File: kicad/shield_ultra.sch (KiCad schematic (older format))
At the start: 12 parts, among them J1 Ultrason, J2 IR, J3 Accel, J4 IR, J5 Ultrason, J6 IR, J7 Ultrason, J8 Ultrason, J9 Ultrason, U1 Conn_shield

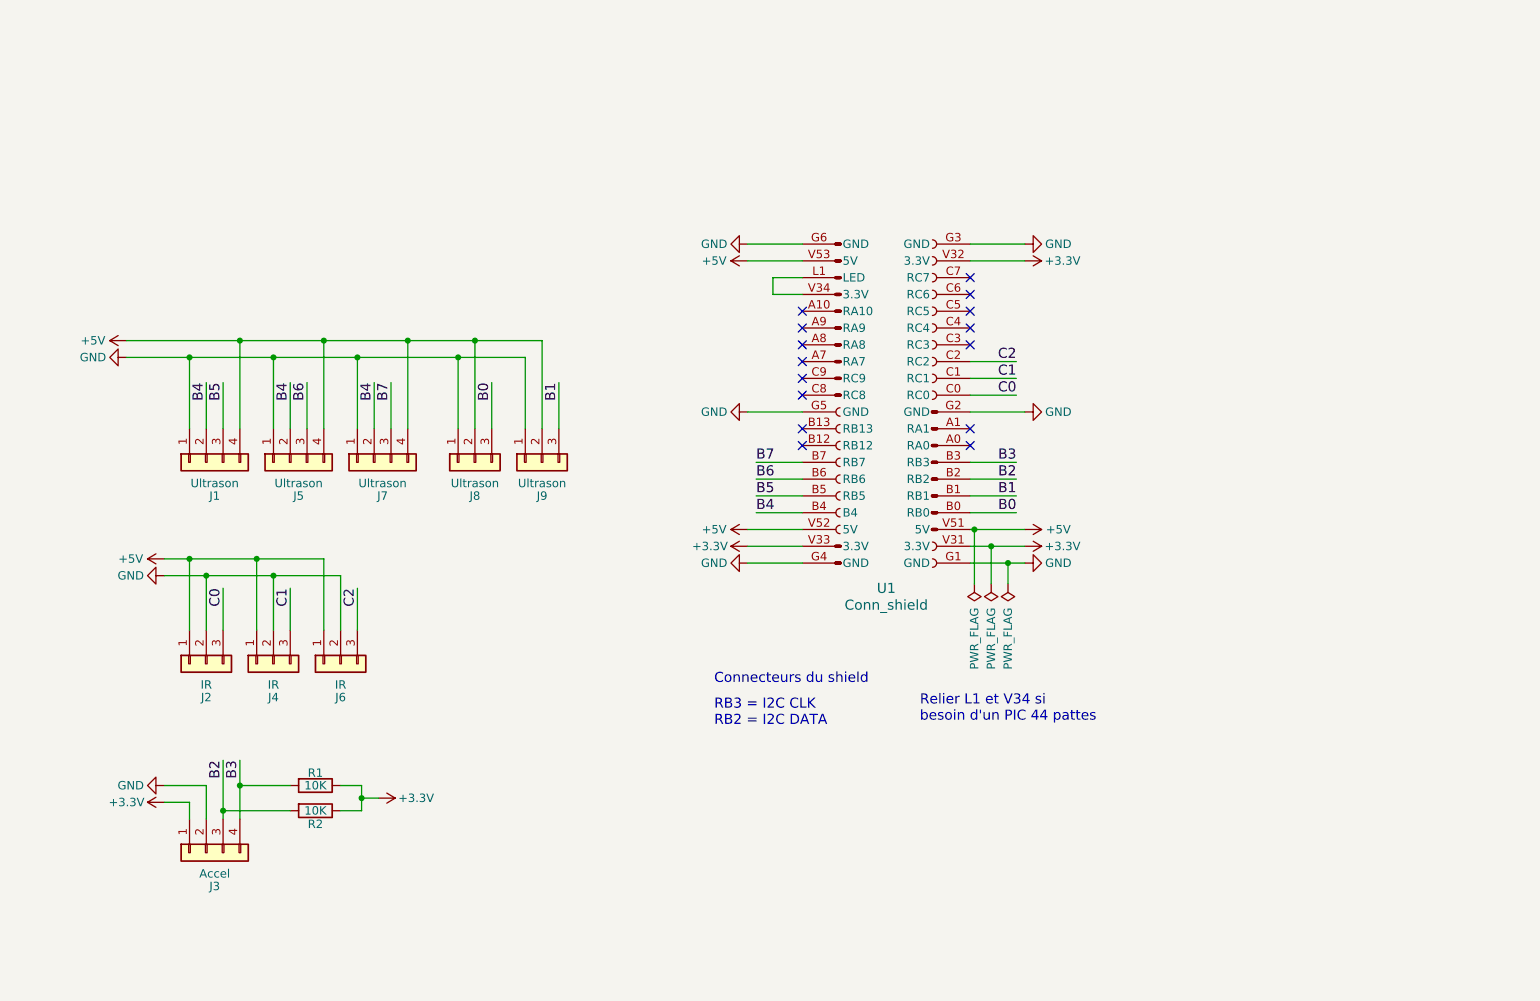
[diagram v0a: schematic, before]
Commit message: Modification connexions capteurs
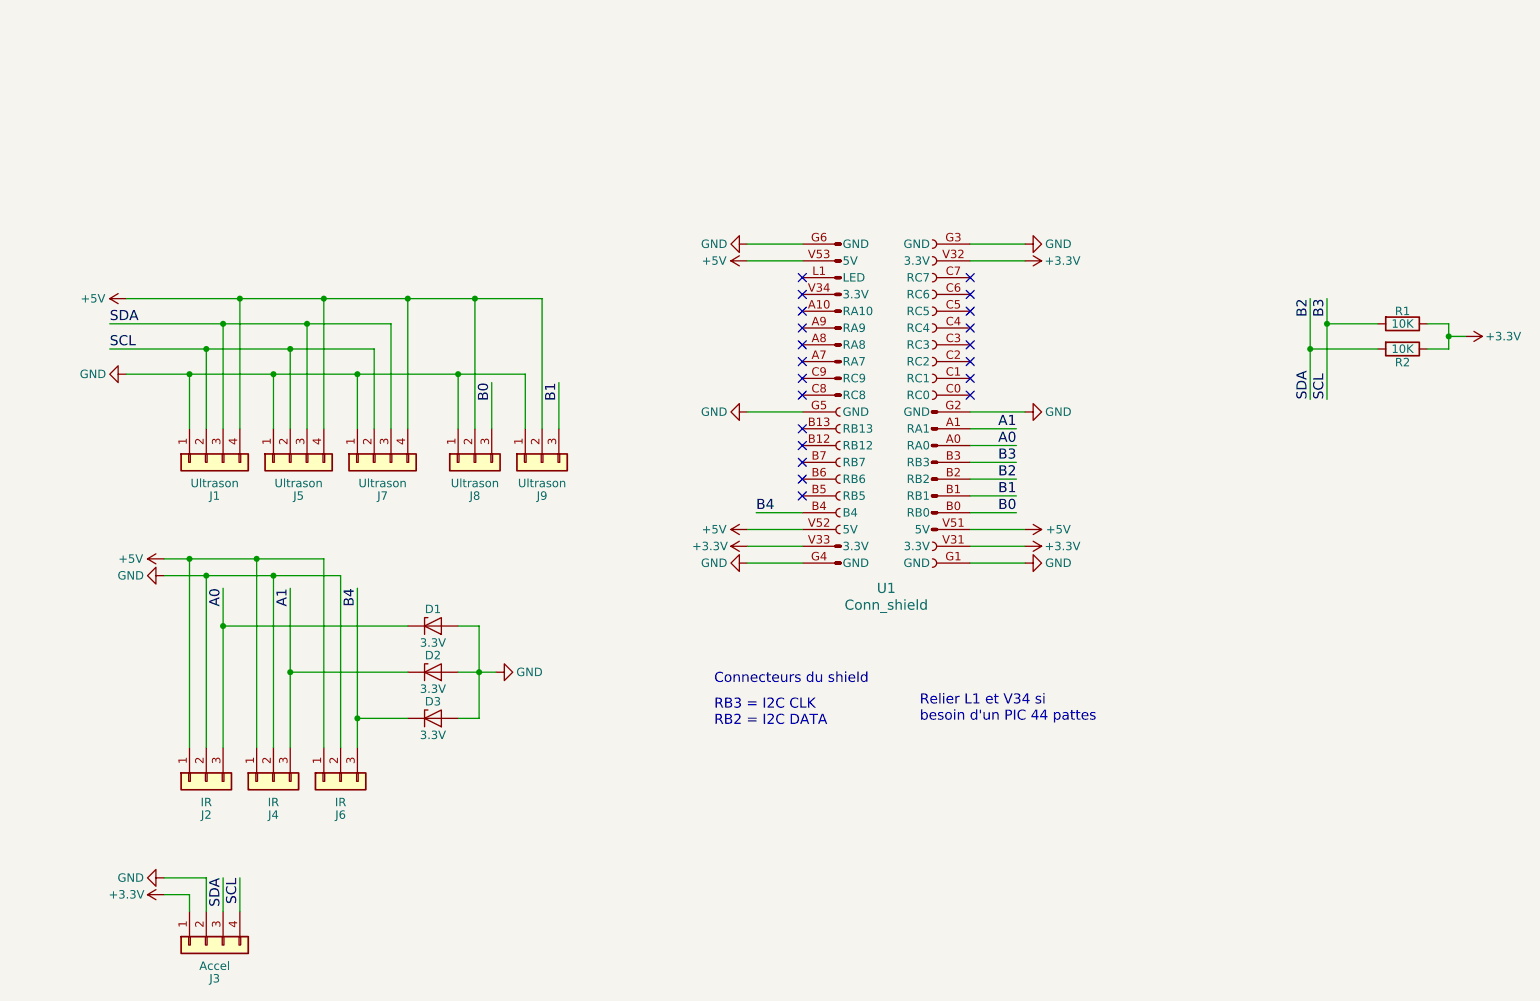
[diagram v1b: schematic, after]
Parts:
- added D1, D2, D3: 3.3V, Diodes_THT:D_A-405_P10.16mm_Horizontal, symbol D_Zener
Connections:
- net B2: now also J1.3 (Pin_3), J5.3 (Pin_3), J7.3 (Pin_3)
- net B3: now also J1.2 (Pin_2), J5.2 (Pin_2), J7.2 (Pin_2)
- net B4: now also J6.3 (Pin_3), D3.1 (K); no longer J1.2 (Pin_2), J5.2 (Pin_2), J7.2 (Pin_2)
- net GND: now also D1.2 (A), D2.2 (A), D3.2 (A)
- net A0: now reaches U1.A0 (RA0)
- net A0: now also J2.3 (Pin_3), D1.1 (K)
- net A1: now reaches U1.A1 (RA1)
- net A1: now also J4.3 (Pin_3), D2.1 (K)
- net at U1.L1 (LED): no longer U1.V34 (3.3V)
- net B5: no longer names the net of U1.B5 (RB5)
- net B5: no longer J1.3 (Pin_3)
- net B6: no longer names the net of U1.B6 (RB6)
- net B6: no longer J5.3 (Pin_3)
- net B7: no longer names the net of U1.B7 (RB7)
- net B7: no longer J7.3 (Pin_3)
- net C0: no longer names the net of U1.C0 (RC0)
- net C0: no longer J2.3 (Pin_3)
- net C1: no longer names the net of U1.C1 (RC1)
- net C1: no longer J4.3 (Pin_3)
- net C2: no longer names the net of U1.C2 (RC2)
- net C2: no longer J6.3 (Pin_3)
- no-connect marks 15 -> 21
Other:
- moved on the sheet: J2, J3, J4, J6, R1, R2

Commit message: Finitions avant release
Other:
- note added: "Connexion des capteurs"
- note added: "Pull up I2C"
- moved on the sheet: D1, D2, D3, J1, J2, J3, J4, J5, J6, J7, J8, J9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
